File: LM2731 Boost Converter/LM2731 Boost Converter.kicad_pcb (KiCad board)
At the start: 2 copper layers, 18 parts, among them J1 USB_C_Receptacle_PowerOnly_6P, U1 LM2731YMF

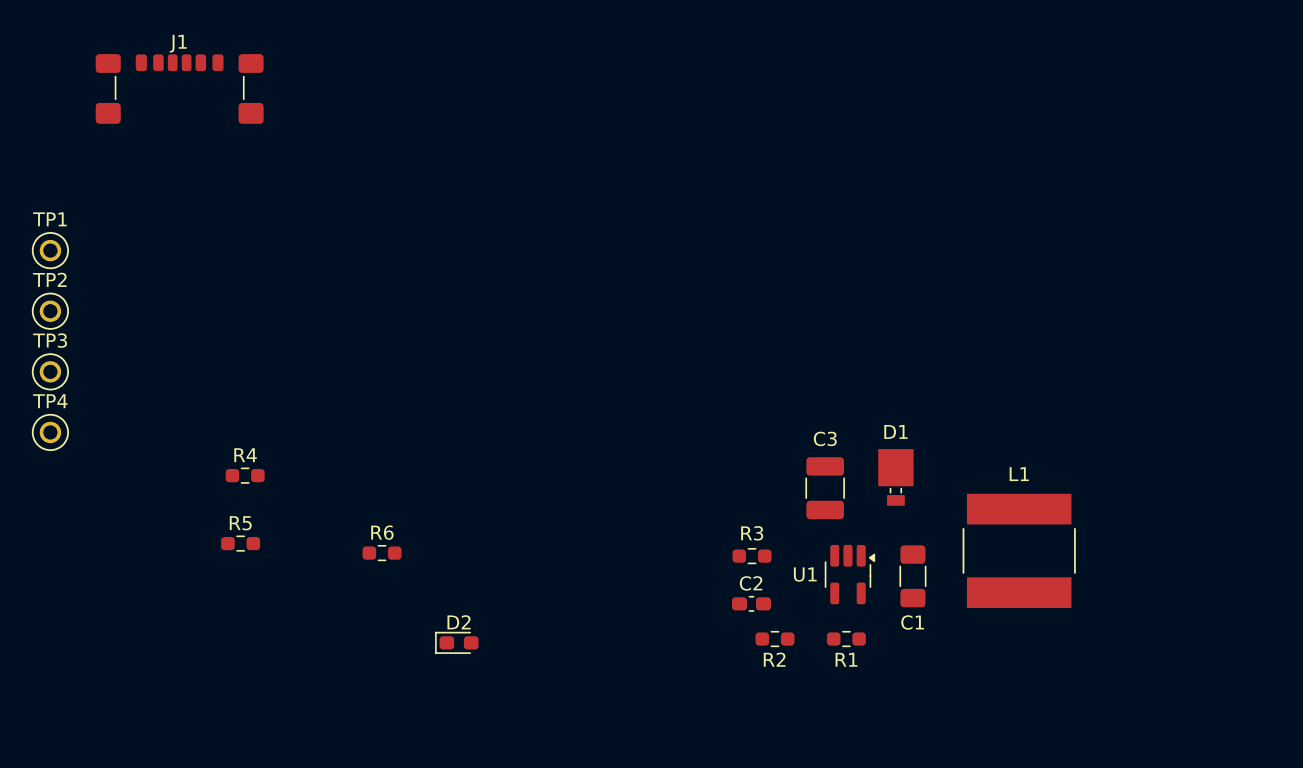
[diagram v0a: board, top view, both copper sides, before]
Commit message: Laid out parts and added a output screw terminal.
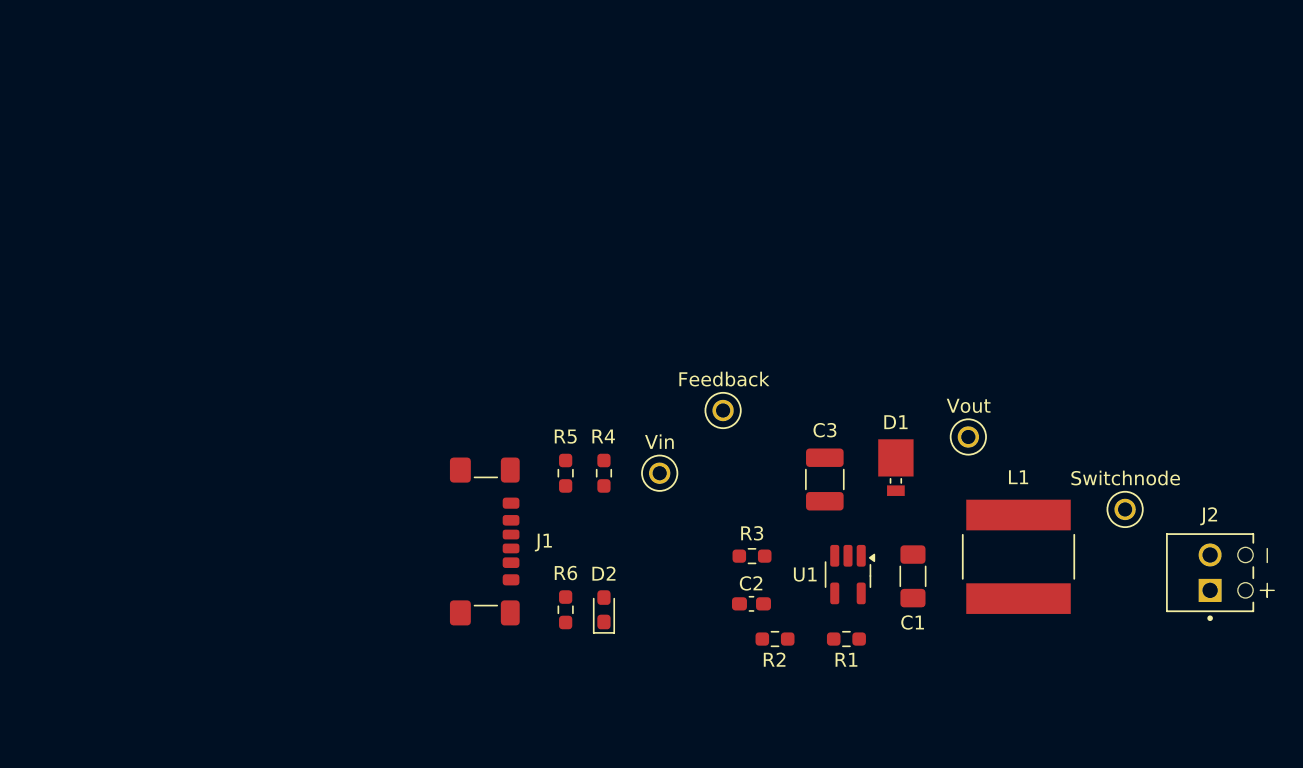
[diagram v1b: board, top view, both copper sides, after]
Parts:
- added J2: Screw_Terminal_01x02, TerminalBlock_Phoenix:PHOENIX_1725656, F.Cu at (122.8, 65.0)
- Vin: renamed from TP1; value TestPoint -> Vin
- moved Switchnode 77.8 mm to (113.5, 57.7)
- moved Vout 66.5 mm to (102.3, 52.5)
- moved Feedback 48.3 mm to (84.7, 50.6)
- moved Vin 46.6 mm to (80.2, 55.1)
- moved J1 37.6 mm to (66.5, 60.0), turned to -90 degrees
- moved R4 25.8 mm to (76.2, 55.1), turned to 90 degrees
- moved R5 23.9 mm to (73.4, 55.1), turned to 90 degrees
- moved R6 13.8 mm to (73.4, 64.9), turned to -90 degrees
- moved D2 10.7 mm to (76.2, 64.9), turned to 90 degrees
- moved D1 0.70 mm to (97.1, 54.7)
- moved C3 0.63 mm to (92.0, 55.5)
- moved L1 0.43 mm to (105.9, 61.1), turned to 90 degrees
- renumbered TP4 to Feedback, TP3 to Switchnode, TP2 to Vout
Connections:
- C1 pad 1: Net-(U1-VIN) -> /Vin
- C2 pad 2: Net-(U1-FB) -> /Feedback
- D1 pad 2: Net-(D1-A) -> /SwitchNode
- Feedback pad TP: (no net) -> /Feedback
- J1 pad A9: Net-(U1-VIN) -> /Vin
- J1 pad B9: Net-(U1-VIN) -> /Vin
- L1 pad 1: Net-(U1-VIN) -> /Vin
- L1 pad 2: Net-(D1-A) -> /SwitchNode
- R1 pad 1: Net-(U1-VIN) -> /Vin
- R2 pad 1: Net-(U1-FB) -> /Feedback
- R3 pad 1: Net-(U1-FB) -> /Feedback
- R6 pad 2: Net-(U1-VIN) -> /Vin
- Switchnode pad TP: (no net) -> /SwitchNode
- U1 pad 1: Net-(D1-A) -> /SwitchNode
- U1 pad 3: Net-(U1-FB) -> /Feedback
- U1 pad 5: Net-(U1-VIN) -> /Vin
- Vin pad TP: (no net) -> /Vin
- Vout pad TP: (no net) -> /Vout

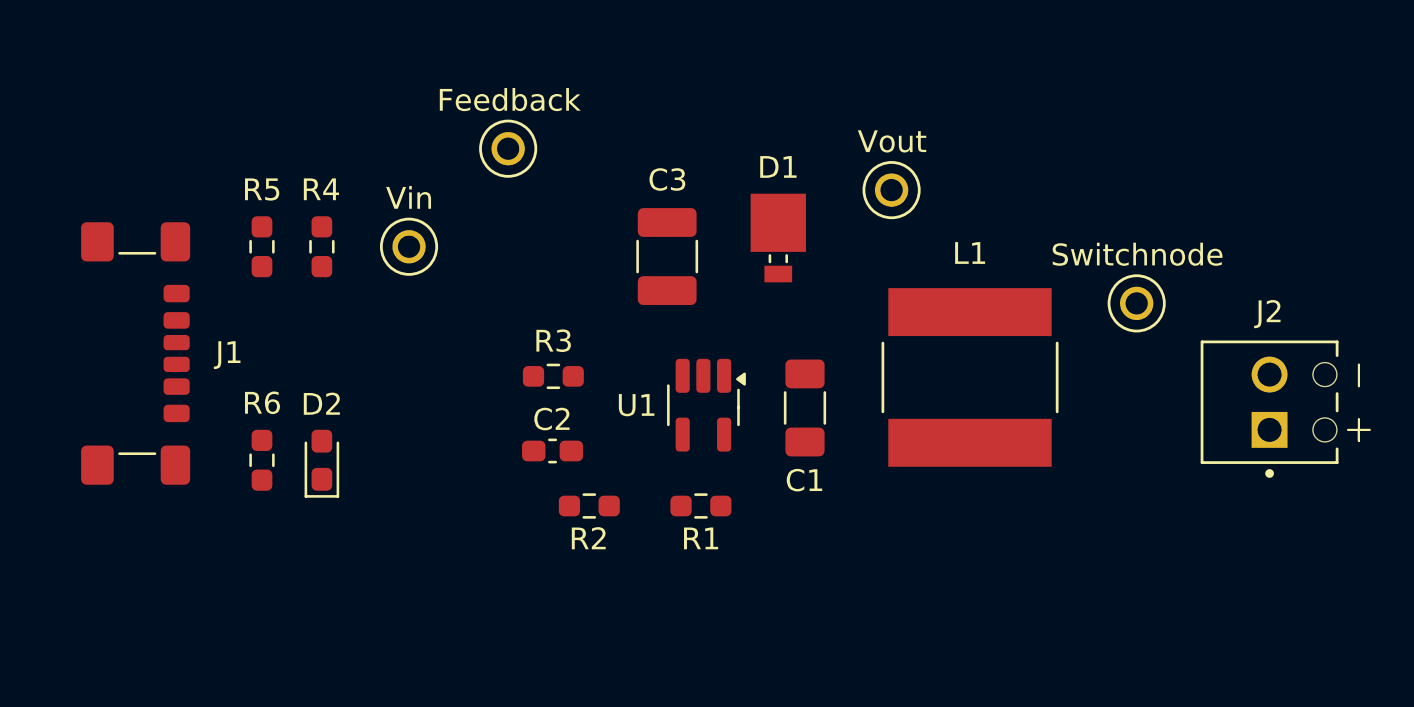
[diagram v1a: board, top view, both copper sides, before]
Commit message: Started routing and placing planes on the PCB.
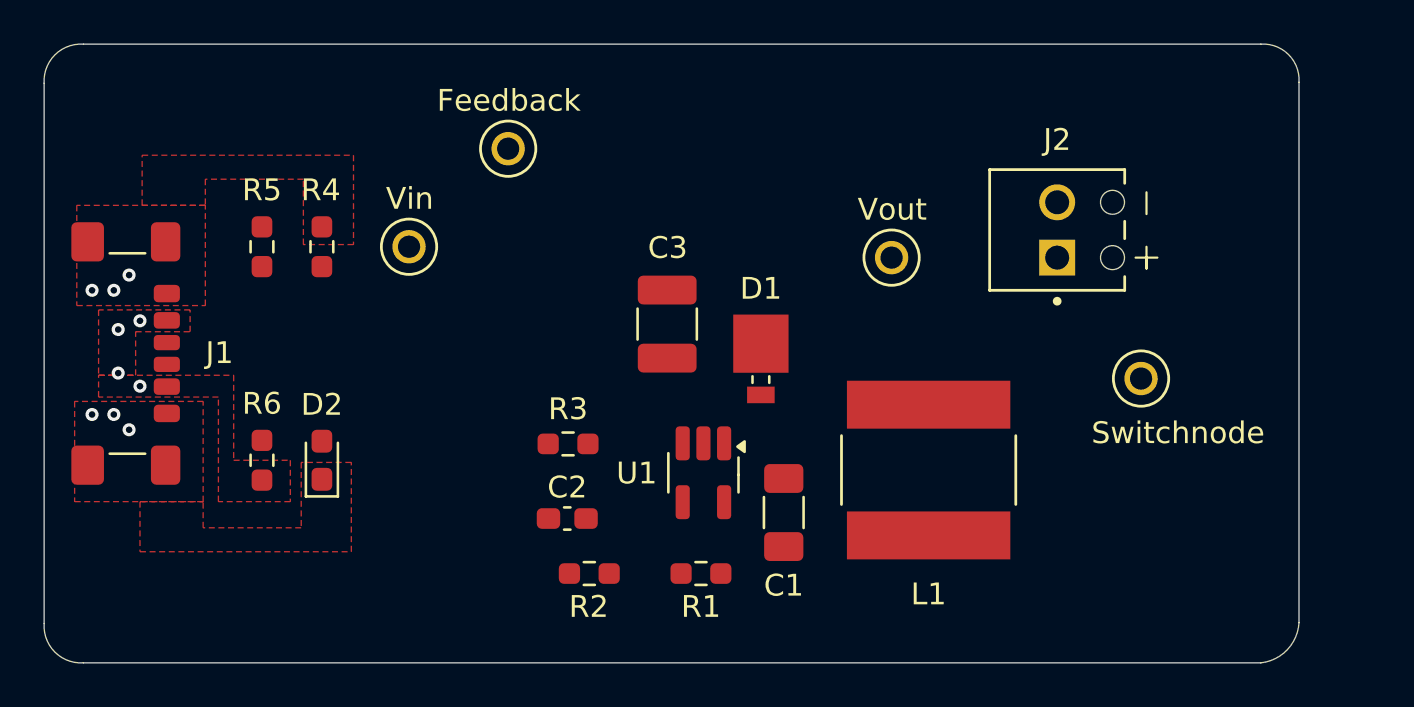
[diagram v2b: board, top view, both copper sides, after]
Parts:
- moved J2 12.6 mm to (113.0, 57.1)
- moved D1 5.60 mm to (96.3, 60.2)
- moved C1 4.90 mm to (97.3, 67.3)
- moved L1 4.66 mm to (104.0, 65.3)
- moved Switchnode 3.46 mm to (113.8, 61.1)
- moved C2 3.17 mm to (87.4, 67.6)
- moved R3 3.17 mm to (87.5, 64.2)
- moved C3 3.10 mm to (92.0, 58.6)
- moved Vout 3.10 mm to (102.3, 55.6)
- moved R1 3.10 mm to (93.5, 70.1)
- moved R2 3.10 mm to (88.4, 70.1)
- moved U1 3.10 mm to (93.7, 65.5)
- moved J1 0.45 mm to (66.0, 60.0)
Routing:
- net GND: vias 0 -> 6
- net /Vin: vias 0 -> 4
- added copper zone on F.Cu, net /Vin
- added copper zone on In2.Cu, net /Vin
- added copper zone on F.Cu, net GND
- added copper zone on In1.Cu, net GND
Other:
- board outline added: 57.6 x 28.4 mm
- copper layers 2 -> 4

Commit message: Finished board layout.
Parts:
- U1: footprint Package_TO_SOT_SMD:SOT-23-5_HandSoldering -> Package_TO_SOT_SMD:SOT-23-5
- moved Feedback 19.3 mm to (81.7, 69.7)
- moved Vin 4.04 mm to (81.2, 59.0)
- moved Switchnode 1.53 mm to (112.8, 62.4)
- moved D1 1.25 mm to (96.8, 59.1)
- moved R2 0.78 mm to (89.2, 70.1)
- moved C1 0.30 mm to (97.3, 67.0)
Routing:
- net Net-(J1-CC2): track 0.00 -> 8.98 mm
- net /SwitchNode: track 0.00 -> 8.80 mm
- net /Vout: track 0.00 -> 7.60 mm
- net /Feedback: track 0.00 -> 6.75 mm
- net Net-(J1-CC1): track 0.00 -> 5.81 mm
- net Net-(D2-A): track 0.00 -> 2.77 mm
- net GND: vias 6 -> 7
- net /Vin: vias 4 -> 8
- added copper zone on F.Cu, net /Feedback
- added copper zone on F.Cu, net /SwitchNode
- added copper zone on F.Cu, net /Vout
